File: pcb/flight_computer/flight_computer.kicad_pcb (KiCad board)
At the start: 4 copper layers, 70 x 45 mm, 82 parts, among them J1 2S pack: XT30 pigtail, 18 AWG, J10 debug UART, J3 SWD (ARM 10-pin 1.27mm), J4 USB-C, J5 u.FL GNSS ant, J6 servo 1 (raw 2S), J7 servo 2 (raw 2S), J8 servo 3 (raw 2S), J9 servo 4 (raw 2S), SW1 reset, U1 TPS62162DSGT, U2 STM32F405RGT6, U3 USBLC6-2SC6, U4 ICM-42688-P, U5 MMC5983MA, U6 MS5611-01BA03, U7 W25Q128JVSIQ, U8 MAX-M10S, U9 LP2985-33DBVR, Y1 8MHz

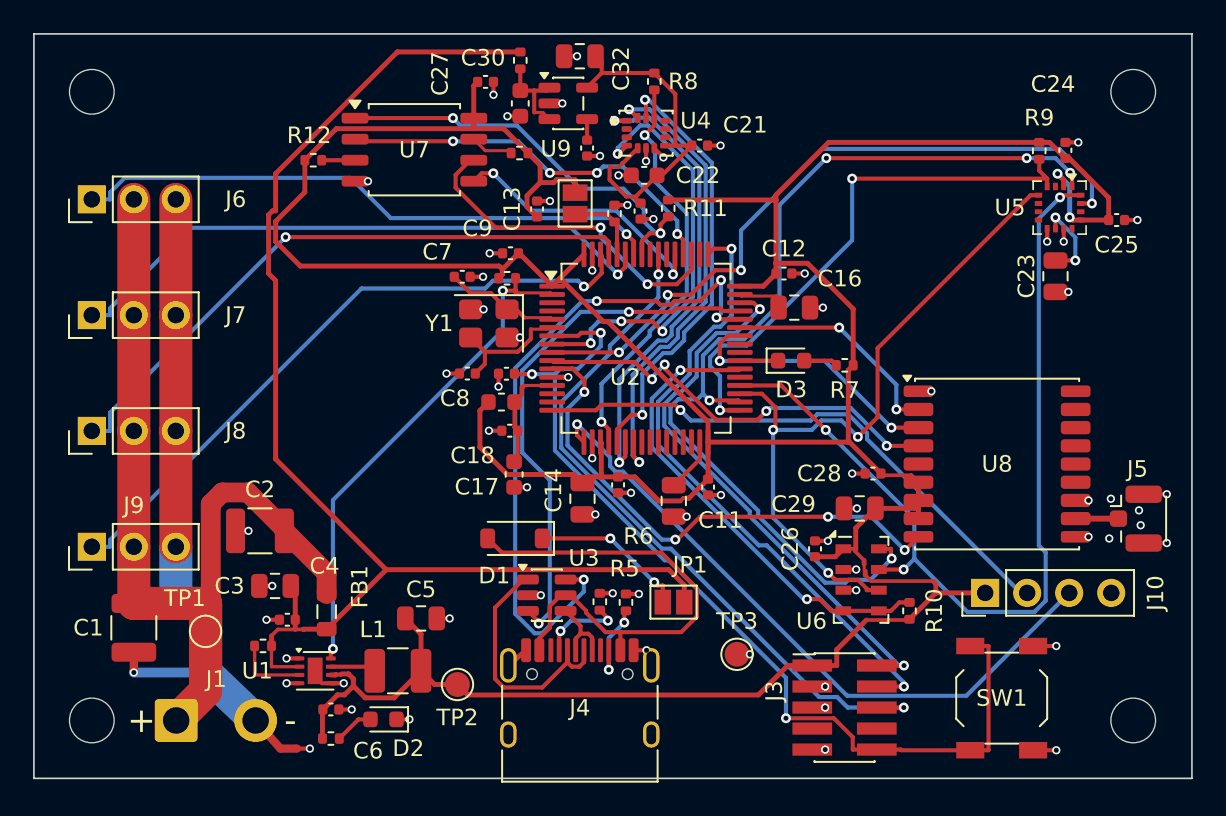
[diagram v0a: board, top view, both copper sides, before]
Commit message: Flight computer: pack-voltage sense, BOM re-verified, pre-fab audit
- PA0 reads the 2S pack through R34/R35 (100k/33k) + C33; nothing could before.
- 32 of 39 BOM lines confirmed on LCSC product pages; SW1 -> TL3342F160QG
  (C2886898) since the reel part is out of stock.
- R8 pinned in layout.py MANUAL_FIXUP after relax() threw it 20.8 mm.
- pcb/README.md 'What is not done' rewritten as the pre-order / bring-up list,
  including the mated-servo-plug height vs the 12 mm packing envelope.
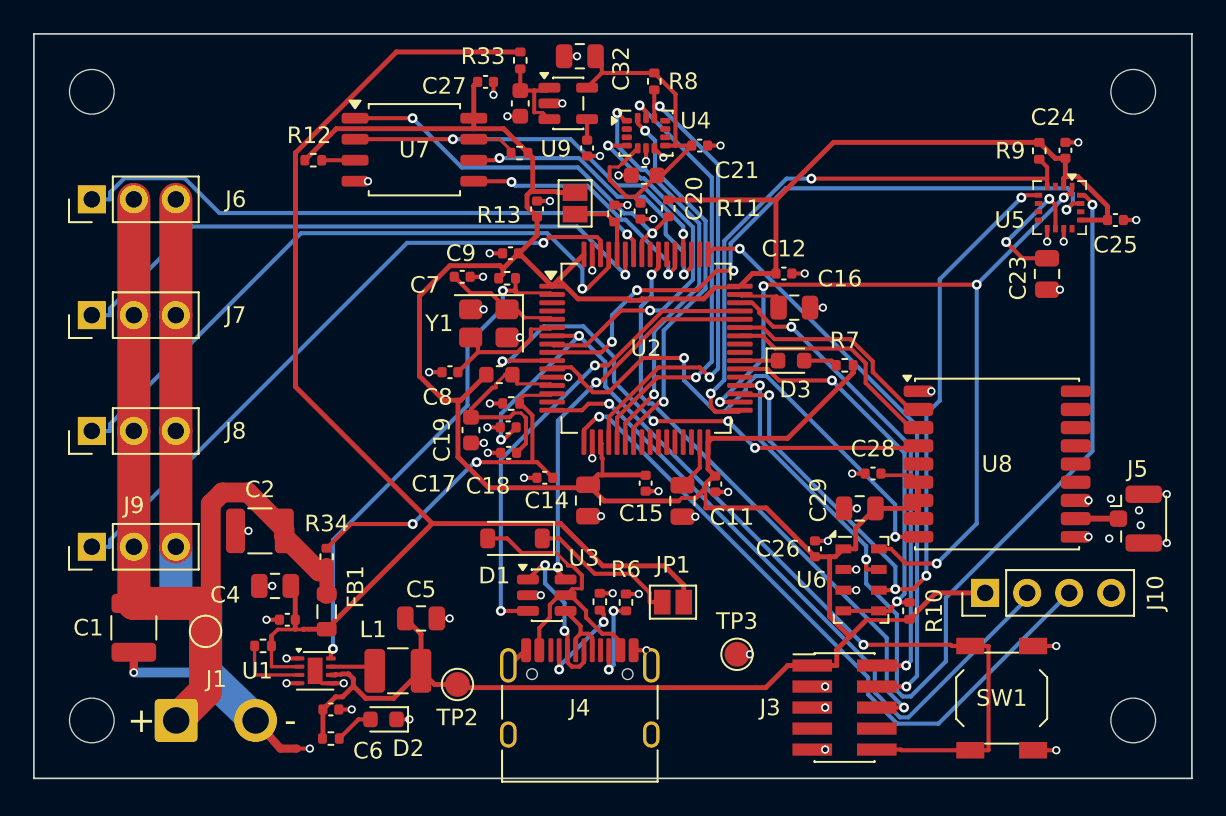
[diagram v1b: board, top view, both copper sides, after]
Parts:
- removed the J5 at (167.1, 129.3)
- removed the J6 at (103.5, 110.0)
- removed the J7 at (103.5, 117.0)
- removed the JP2 at (132.7, 110.2)
- removed the SW1 at (158.5, 140.2)
- removed the U2 at (137.0, 119.0)
- removed the U3 at (131.0, 133.9)
- removed the U6 at (150.0, 133.0)
- removed the U7 at (123.0, 107.0)
- added C28: 100nF, Capacitor_SMD:C_0402_1005Metric, F.Cu at (150.7, 126.6)
- added C29: 10uF, Capacitor_SMD:C_0805_2012Metric, F.Cu at (149.9, 128.7)
- added J10: debug UART, Connector_PinHeader_2.54mm:PinHeader_1x04_P2.54mm_Vertical, F.Cu at (157.5, 133.8)
- added J3: SWD (ARM 10-pin 1.27mm), Connector_PinHeader_1.27mm:PinHeader_2x05_P1.27mm_Vertical_SMD, F.Cu at (149.0, 140.7)
- added J8: servo 3 (raw 2S), Connector_PinHeader_2.54mm:PinHeader_1x03_P2.54mm_Vertical, F.Cu at (103.5, 124.0)
- added J9: servo 4 (raw 2S), Connector_PinHeader_2.54mm:PinHeader_1x03_P2.54mm_Vertical, F.Cu at (103.5, 131.0)
- added R13: 10k, Resistor_SMD:R_0402_1005Metric, F.Cu at (129.4, 107.2)
- added R33: 10, Resistor_SMD:R_0402_1005Metric, F.Cu at (129.4, 101.6)
- added R34: 100k, Resistor_SMD:R_0402_1005Metric, F.Cu at (117.7, 131.6)
- added R35: 33k, Resistor_SMD:R_0402_1005Metric, F.Cu at (128.8, 122.3)
- added R7: 1k, Resistor_SMD:R_0402_1005Metric, F.Cu at (149.0, 120.0)
- added U4: ICM-42688-P, Package_LGA:LGA-14_3x2.5mm_P0.5mm_LayoutBorder3x4y, F.Cu at (137.0, 106.0)
- C20: renamed from C23; value 10uF SET/RESET -> 100nF; footprint Capacitor_SMD:C_0805_2012Metric -> Capacitor_SMD:C_0402_1005Metric
- C22: renamed from C25; value 100nF -> 2.2uF; footprint Capacitor_SMD:C_0402_1005Metric -> Capacitor_SMD:C_0603_1608Metric
- C23: renamed from C26; value 100nF -> 10uF SET/RESET; footprint Capacitor_SMD:C_0402_1005Metric -> Capacitor_SMD:C_0805_2012Metric
- C25: renamed from C30; value 1uF -> 100nF; footprint Capacitor_SMD:C_0603_1608Metric -> Capacitor_SMD:C_0402_1005Metric
- C26: renamed from C31; value 10nF -> 100nF
- C27: renamed from C32; value 4.7uF -> 100nF; footprint Capacitor_SMD:C_0805_2012Metric -> Capacitor_SMD:C_0402_1005Metric
- C30: renamed from R8; value 10k -> 1uF; footprint Resistor_SMD:R_0402_1005Metric -> Capacitor_SMD:C_0603_1608Metric
- C31: renamed from R9; value 10k -> 10nF; footprint Resistor_SMD:R_0402_1005Metric -> Capacitor_SMD:C_0402_1005Metric
- C32: renamed from R10; value 10k -> 4.7uF; footprint Resistor_SMD:R_0402_1005Metric -> Capacitor_SMD:C_0805_2012Metric
- C33: renamed from D3; value blue -> 100nF; footprint LED_SMD:LED_0603_1608Metric -> Capacitor_SMD:C_0402_1005Metric
- D3: renamed from FB2; value 600R@100MHz -> blue; footprint Inductor_SMD:L_0603_1608Metric -> LED_SMD:LED_0603_1608Metric
- FB2: renamed from J3; value SWD (ARM 10-pin 1.27mm) -> 600R@100MHz; footprint Connector_PinHeader_1.27mm:PinHeader_2x05_P1.27mm_Vertical_SMD -> Inductor_SMD:L_0603_1608Metric
- J5: renamed from J8; value servo 3 (raw 2S) -> u.FL GNSS ant; footprint Connector_PinHeader_2.54mm:PinHeader_1x03_P2.54mm_Vertical -> Connector_Coaxial:U.FL_Hirose_U.FL-R-SMT-1_Vertical
- J6: renamed from J9; value servo 4 (raw 2S) -> servo 1 (raw 2S)
- J7: renamed from J10; value debug UART -> servo 2 (raw 2S); footprint Connector_PinHeader_2.54mm:PinHeader_1x04_P2.54mm_Vertical -> Connector_PinHeader_2.54mm:PinHeader_1x03_P2.54mm_Vertical
- JP2: renamed from R4; value 10k -> BOOT0->3V3 (open); footprint Resistor_SMD:R_0402_1005Metric -> Jumper:SolderJumper-2_P1.3mm_Open_Pad1.0x1.5mm
- R11: renamed from R33; value 10 -> 10k
- R12: renamed from U4; value ICM-42688-P -> 10k; footprint Package_LGA:LGA-14_3x2.5mm_P0.5mm_LayoutBorder3x4y -> Resistor_SMD:R_0402_1005Metric
- R4: renamed from R5; value 5.1k -> 10k
- R6: renamed from R7; value 1k -> 5.1k
- SW1: renamed from Y1; value 8MHz -> reset; footprint Crystal:Crystal_SMD_3225-4Pin_3.2x2.5mm -> Button_Switch_SMD:SW_SPST_TL3342
- U2: renamed from C20; value 100nF -> STM32F405RGT6; footprint Capacitor_SMD:C_0402_1005Metric -> Package_QFP:LQFP-64_10x10mm_P0.5mm
- U3: renamed from C21; value 100nF -> USBLC6-2SC6; footprint Capacitor_SMD:C_0402_1005Metric -> Package_TO_SOT_SMD:SOT-23-6
- U6: renamed from C28; value 100nF -> MS5611-01BA03; footprint Capacitor_SMD:C_0402_1005Metric -> Package_LGA:LGA-8_3x5mm_P1.25mm
- U7: renamed from C29; value 10uF -> W25Q128JVSIQ; footprint Capacitor_SMD:C_0805_2012Metric -> Package_SO:SOIC-8_5.3x5.3mm_P1.27mm
- Y1: renamed from C22; value 2.2uF -> 8MHz; footprint Capacitor_SMD:C_0603_1608Metric -> Crystal:Crystal_SMD_3225-4Pin_3.2x2.5mm
- moved J5 63.8 mm to (167.1, 129.3), turned to 0 degrees
- moved J7 56.6 mm to (103.5, 117.0)
- moved R9 43.9 mm to (160.8, 107.1), turned to -90 degrees
- moved C32 39.0 mm to (133.0, 101.3), turned to 180 degrees
- moved SW1 38.4 mm to (158.5, 140.2), turned to 90 degrees
- moved C25 36.7 mm to (165.4, 111.2), turned to 0 degrees
- moved R10 36.4 mm to (152.9, 134.9), turned to 90 degrees
- moved C24 35.3 mm to (162.4, 107.0), turned to 90 degrees
- moved U7 34.6 mm to (123.0, 107.0), turned to 0 degrees
- moved FB2 29.0 mm to (128.1, 120.6)
- moved U3 28.7 mm to (131.0, 133.9)
- moved C22 28.7 mm to (136.9, 108.5), turned to 180 degrees
- moved C26 27.9 mm to (147.2, 131.1), turned to 90 degrees
- moved C31 27.3 mm to (133.4, 106.9)
- moved C20 25.4 mm to (136.7, 110.7)
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- renumbered C24 to C21, C27 to C24, R13 to R10, R6 to R5, R11 to R8, R12 to R9
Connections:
- C20 pad 1: MAG_CAP -> +3V3_IMU
- C21 pad 1: +3V3 -> +3V3_IMU
- C22 pad 1: +3V3 -> +3V3_IMU
- C23 pad 1: +3V3 -> MAG_CAP
- C25 pad 1: VIN_IMU -> +3V3
- C26 pad 1: IMU_LDO_BP -> +3V3
- C27 pad 1: +3V3_IMU -> +3V3
- C30 pad 1: +3V3_IMU -> VIN_IMU
- C30 pad 2: CS1_IMU -> GND
- C31 pad 1: +3V3 -> IMU_LDO_BP
- C31 pad 2: CS2_MAG -> GND
- C32 pad 1: +3V3 -> +3V3_IMU
- C32 pad 2: CS3_BARO -> GND
- C33 pad 1: LED_STAT -> VBAT_SENSE
- C33 pad 2: LED_STAT_A -> GND
- D3 pad 1: +3V3 -> LED_STAT
- D3 pad 2: VDDA -> LED_STAT_A
- FB2 pad 2: SWDIO -> VDDA
- J5 pad 1: SERVO3 -> GNSS_RF
- J5 pad 2: VBATT -> GND
- J6 pad 1: SERVO4 -> SERVO1
- J7 pad 1: +3V3 -> SERVO2
- J7 pad 2: DBG_TX -> VBATT
- J7 pad 3: DBG_RX -> SERVO_GND
- JP2 pad 2: GND -> +3V3
- R10 pad 2: FLASH_HOLD -> CS3_BARO
- R11 pad 1: VIN -> +3V3
- R11 pad 2: VIN_IMU -> CS4_FLASH
- R12 pad 1: SPI1_MISO -> +3V3
- R12 pad 2: unconnected-(U4-RESV2-Pad2) -> FLASH_WP
- R4 pad 1: USB_CC1 -> BOOT0
- R5 pad 1: USB_CC2 -> USB_CC1
- R6 pad 1: +3V3 -> USB_CC2
- R6 pad 2: LED_STAT_A -> GND
- R8 pad 1: +3V3 -> +3V3_IMU
- R8 pad 2: CS4_FLASH -> CS1_IMU
- R9 pad 2: FLASH_WP -> CS2_MAG
- SW1 pad 1: OSC_IN -> NRST
- U2 pad 1: +3V3_IMU -> +3V3
- U2 pad 2: GND -> PGOOD
- U3 pad 1: +3V3_IMU -> USB_DM_CON
- U7 pad 1: +3V3 -> CS4_FLASH
- U7 pad 2: GND -> SPI3_MISO
- Y1 pad 1: +3V3_IMU -> OSC_IN
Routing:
- net VBAT_SENSE: track 0.00 -> 22.4 mm, vias 0 -> 2
- net USB_DM: track 41.0 -> 23.3 mm, vias 4 -> 2
- net VBUS: track 30.2 -> 18.1 mm
- net +3V3: track 232.1 -> 222.8 mm, vias 2 -> 0
- net GNSS_TIMEPULSE: track 25.9 -> 33.0 mm
- net SPI2_SCK: track 59.4 -> 52.5 mm
- net DBG_TX: track 34.1 -> 40.9 mm
- net SWO: track 43.0 -> 36.2 mm
- net SPI2_MOSI: track 54.7 -> 60.7 mm
- net VDDA: track 6.80 -> 12.7 mm
- net SPI1_MOSI: track 28.3 -> 23.2 mm
- net USB_DM_CON: track 14.9 -> 9.78 mm, vias 0 -> 2
- net SWDIO: track 34.0 -> 29.2 mm
- net CS1_IMU: track 24.9 -> 29.2 mm
- net IMU_INT1: track 25.8 -> 21.7 mm, vias 4 -> 2
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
